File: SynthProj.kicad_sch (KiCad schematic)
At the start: 32 parts, among them J10 PWM IN, J15 Mixer Ext In, J17 S&H_In, J17 S&H_Out, J20 Ext CV, J9 Lin CV In

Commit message: more work...
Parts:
- removed J?: Master Output, SynthProjConnectors:JINJIA CK3.5-98-LF, symbol SynthProj-rescue:AudioJack2-Connector
- J?: value Master Output -> Gate Out
- J?: value Master Output -> Sequencer CV1
- J?: value Master Output -> Sequencer CV3
- J?: value Master Output -> Sequencer CV2
- J?: value Master Output -> Trigger Out
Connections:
- net SequencerAnalogGenerator/CV1: now also J?.T
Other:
- moved on the sheet: J?

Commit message: finishing schematic 1.0
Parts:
- removed J?: ADEG2_OUT, SynthProjConnectors:JINJIA CK3.5-98-LF, symbol SynthProj-rescue:AudioJack2-Connector
- added J? (x8): Sequencer CV1, SynthProjConnectors:JINJIA CK3.5-98-LF, symbol SynthProj-rescue:AudioJack2-Connector
- J18: renamed from J20; value Ext CV -> Ext In
- J?: value ADEG2_OUT -> Echo_ExtIn
- J?: value ADEG2_OUT -> Echo_DV
- J?: value ADEG2_OUT -> Echo_CV_In
- J?: value ADEG2_OUT -> Echo_Repeat
- renumbered J15 to J?, J17 to J?, J9 to J?, J10 to J?
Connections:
- net GNDREF: now also J?.S, J?.S, J?.S, J?.S, J?.S, J?.S, J?.S, J?.S
- new net RP2040Microcontroller/VIN_A: J?.T
- new net RP2040Microcontroller/VIN_B: J?.T
- new net RP2040Microcontroller/VIN_C: J?.T
- new net RP2040Microcontroller/VIN_D: J?.T
- new net RP2040Microcontroller/VOUT_A: J?.T
- new net RP2040Microcontroller/VOUT_B: J?.T
- new net RP2040Microcontroller/VOUT_C: J?.T
- new net RP2040Microcontroller/VOUT_D: J?.T
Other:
- sheet PT2399Echo ports: added none; removed VCA
- sheet RP2040Microcontroller ports: added VIN_A, VIN_B, VIN_C, VIN_D, VOUT_A, VOUT_B, VOUT_C, VOUT_D; removed none
- note added: "100k 20mm Linear Pot: RK09D1130-F20-C0-B104 100k 20mm Log Pot: RK09D1130-F20-C0-A104 10k 20mm Linear Pot: RK09D1130-F20-C0-B103 10k 20mm Log Pot: RK09D1130-F20-C0-V103"
- note added: "12 Pole Rotary Switch - Metal MC12L1NCQD 9.4mm shoulder height 12 Pole Rotary Switch - Plastic RTAP31S12W25FS 12.6mm shoulder height 12 Pole Rotary Switch - Plastic KC52A10.001NPS 14.2mm shoulder height 12 Pole Rotary Switch - Plastic SR2612F-0112-21R0B-D8-N 12.6mm shoulder height"
- note added: "4 Pole Rotary Switch - SRBV141404"
- note added: "Miniture switches need a panel height of 9.5 to 18.8mm."
- note added: "SPST On-Off MTS-101-A1-T0 SPDT On-On MTS-102-A01-T0 SPDT On-Off-On MTS-103-A1-T0 DPDT On-On MTS-202-A1-T0 DPDT On-Off-On MTS-203-A1-T0 I'm going to use the MTS series because it is a little bigger"
- note added: "SubMiniture switches need a panel height of 8.6 to 14.2mm."
- note added: "The panel height will hopefully be about 14-15mm off the pcb, for a total thickeness of about 16mm, then with knobs and buttons protruding."
- note added: "Vertical Midi Connector SD-50BV - Its 15.8mm tall"
- moved on the sheet: J?

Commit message: Doing some layout
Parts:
- J18, J? (x37): footprint SynthProjConnectors:JINJIA CK3.5-98-LF -> SynthProjConnectors:PJ-358

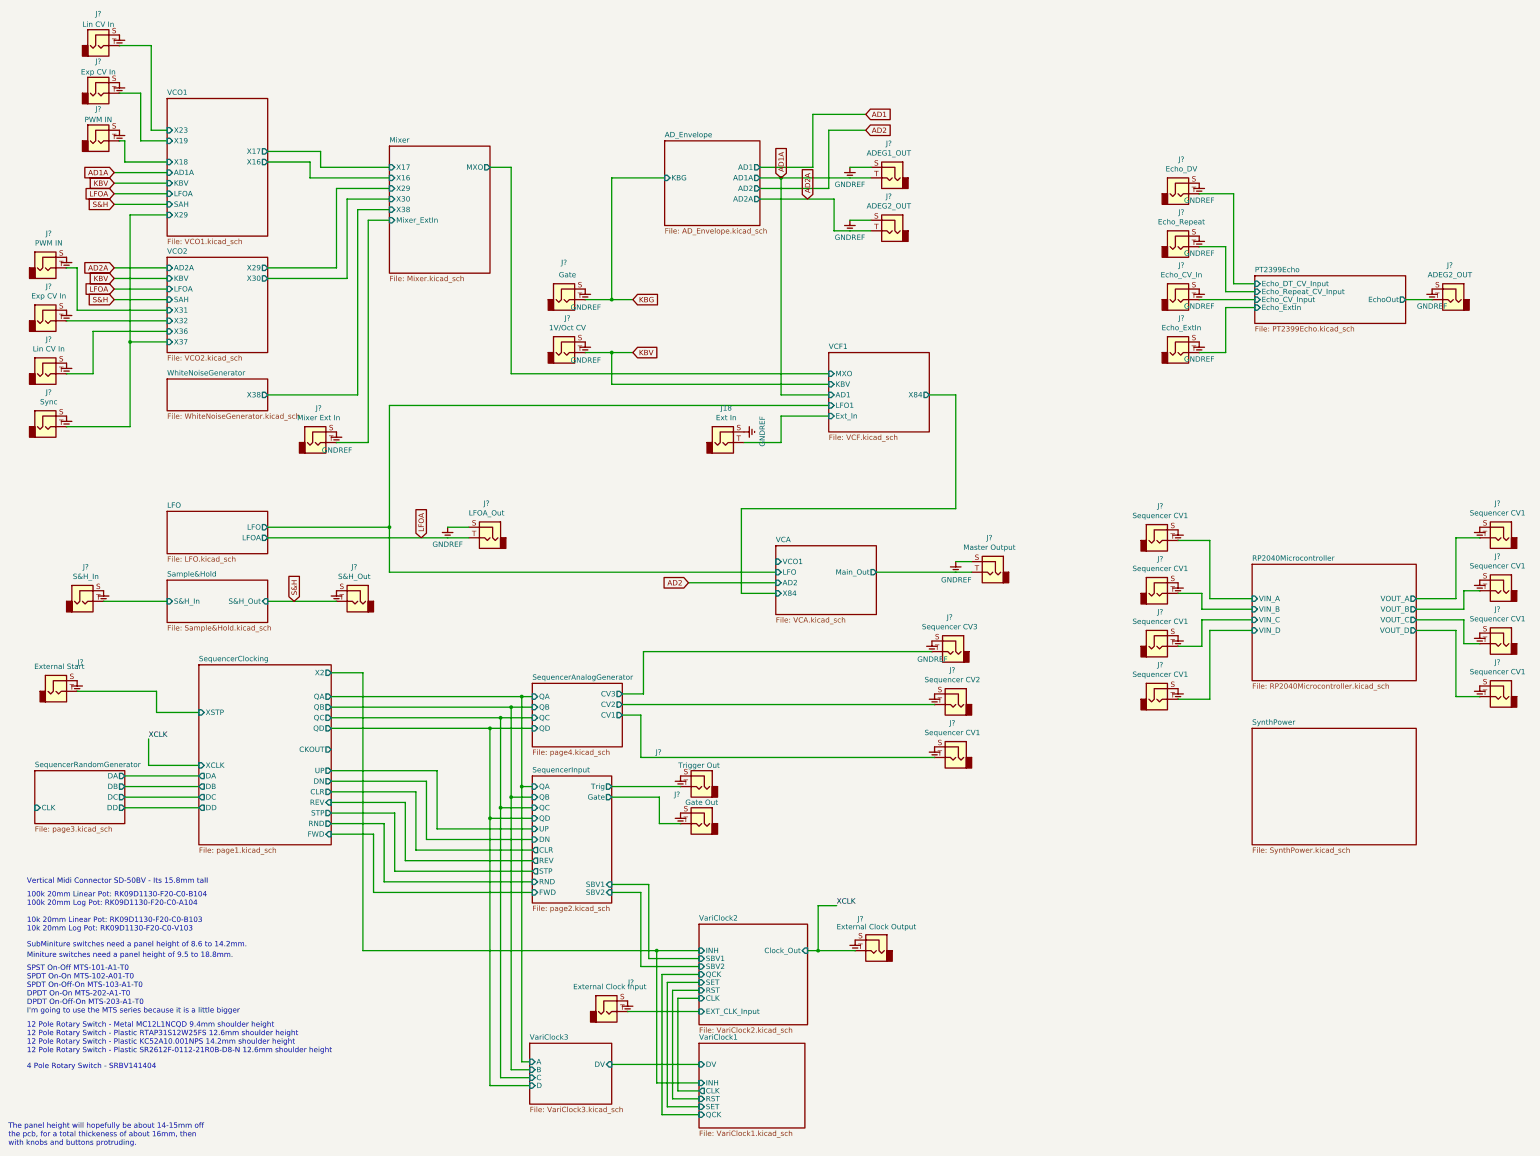
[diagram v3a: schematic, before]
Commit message: doing some routing - split sequencer into another project
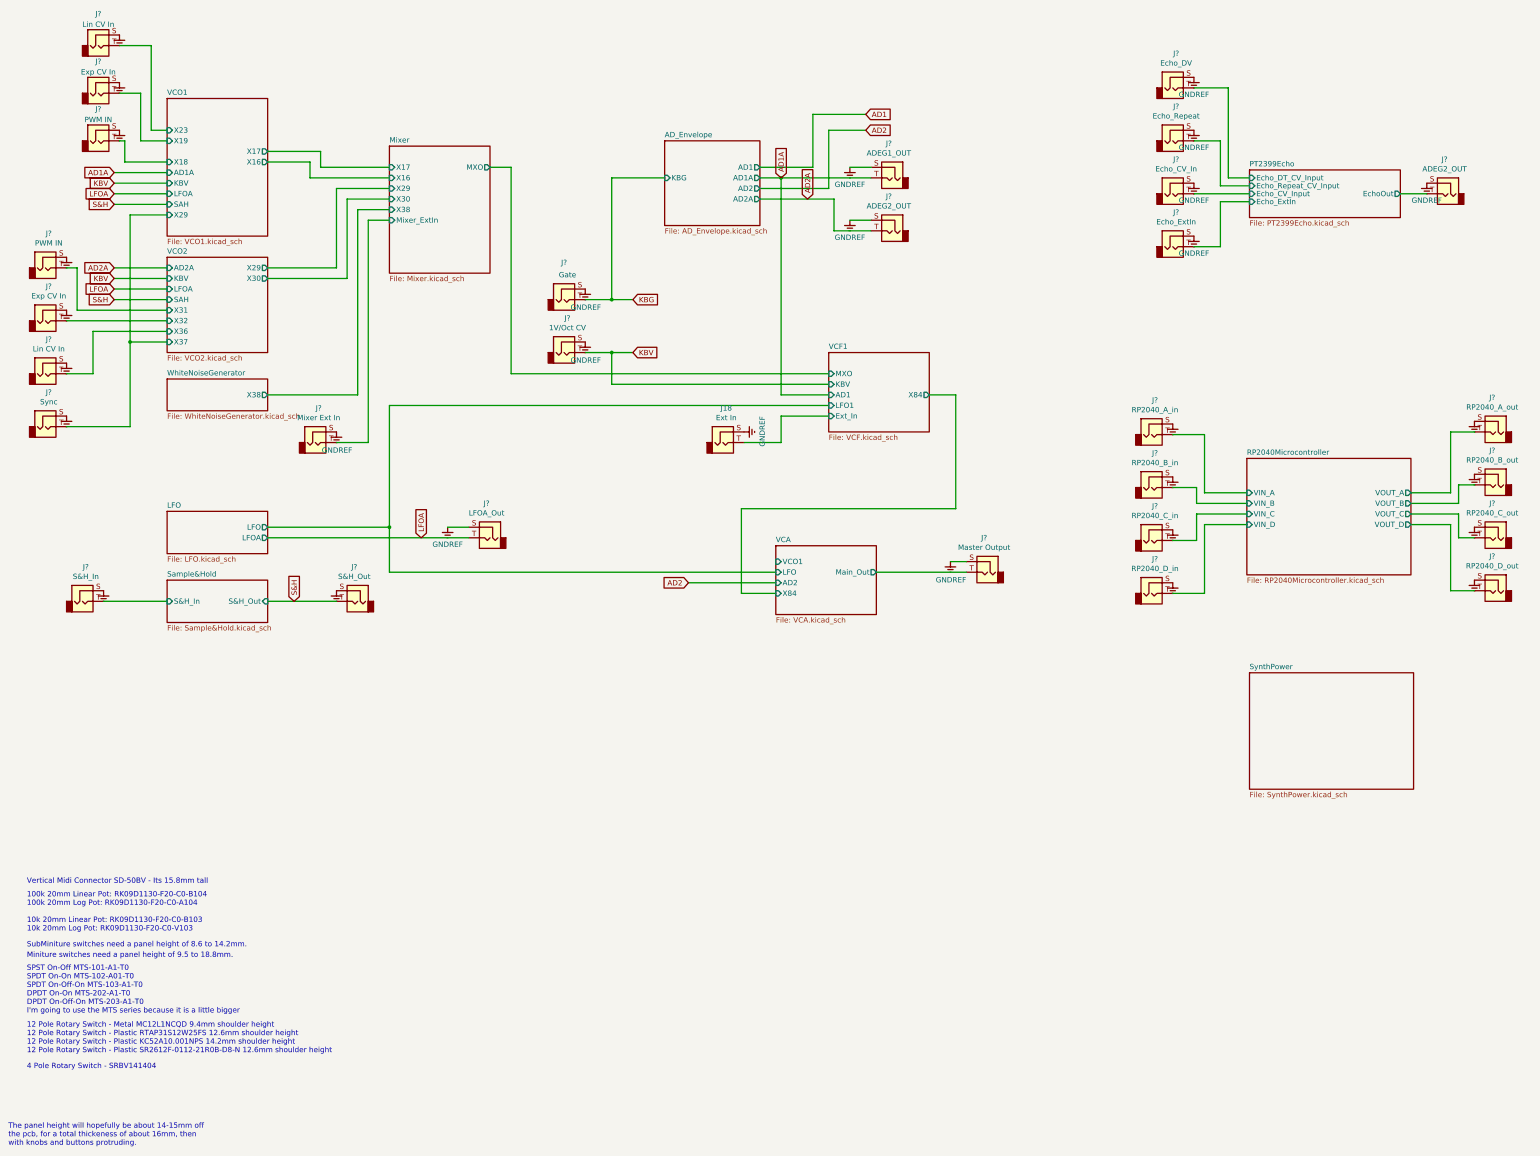
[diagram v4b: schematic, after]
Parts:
- removed J?: External Clock Output, SynthProjConnectors:PJ-358, symbol SynthProj-rescue:AudioJack2-Connector
- removed J?: Gate Out, SynthProjConnectors:PJ-358, symbol SynthProj-rescue:AudioJack2-Connector
- removed J?: Sequencer CV1, SynthProjConnectors:PJ-358, symbol SynthProj-rescue:AudioJack2-Connector
- removed J?: Sequencer CV3, SynthProjConnectors:PJ-358, symbol SynthProj-rescue:AudioJack2-Connector
- removed J?: Sequencer CV2, SynthProjConnectors:PJ-358, symbol SynthProj-rescue:AudioJack2-Connector
- removed J?: Trigger Out, SynthProjConnectors:PJ-358, symbol SynthProj-rescue:AudioJack2-Connector
- removed J?: External Start, SynthProjConnectors:PJ-358, symbol SynthProj-rescue:AudioJack2-Connector
- removed J?: External Clock Input, SynthProjConnectors:PJ-358, symbol SynthProj-rescue:AudioJack2-Connector
- J18, J? (x21): footprint SynthProjConnectors:PJ-358 -> SynthProjConnectors:PJ-301
- J?: value Sequencer CV1 -> RP2040_A_out; footprint SynthProjConnectors:PJ-358 -> SynthProjConnectors:PJ-301
- J?: value Sequencer CV1 -> RP2040_D_in; footprint SynthProjConnectors:PJ-358 -> SynthProjConnectors:PJ-301
- J?: value Sequencer CV1 -> RP2040_C_in; footprint SynthProjConnectors:PJ-358 -> SynthProjConnectors:PJ-301
- J?: value Sequencer CV1 -> RP2040_B_out; footprint SynthProjConnectors:PJ-358 -> SynthProjConnectors:PJ-301
- J?: value Sequencer CV1 -> RP2040_A_in; footprint SynthProjConnectors:PJ-358 -> SynthProjConnectors:PJ-301
- J?: value Sequencer CV1 -> RP2040_C_out; footprint SynthProjConnectors:PJ-358 -> SynthProjConnectors:PJ-301
- J?: value Sequencer CV1 -> RP2040_D_out; footprint SynthProjConnectors:PJ-358 -> SynthProjConnectors:PJ-301
- J?: value Sequencer CV1 -> RP2040_B_in; footprint SynthProjConnectors:PJ-358 -> SynthProjConnectors:PJ-301
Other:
- removed sheet SequencerAnalogGenerator
- removed sheet SequencerClocking
- removed sheet SequencerInput
- removed sheet SequencerRandomGenerator
- removed sheet VariClock1
- removed sheet VariClock2
- removed sheet VariClock3
- moved on the sheet: J?

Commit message: routing work...
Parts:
- removed J?: RP2040_D_in, SynthProjConnectors:PJ-301, symbol SynthProj-rescue:AudioJack2-Connector
- J?: value ADEG2_OUT -> ECHO_OUT
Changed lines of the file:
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@@
 (kicad_sch (version 20230121) (generator eeschema)
-  (paper "A3")
+  (paper "A4")
   (junction (at 105.41 134.62) (diameter 0) (color 0 0 0 0)
   )
@@
     (stroke (width 0) (type default))
   )
-  (wire (pts (xy 311.15 133.985) (xy 300.99 133.985))
-    (stroke (width 0) (type default))
-  )
   (wire (pts (xy 210.82 53.34) (xy 210.82 39.37))
     (stroke (width 0) (type default))
@@
     (stroke (width 0) (type default))
   )
-  (wire (pts (xy 300.99 150.495) (xy 293.37 150.495))
-    (stroke (width 0) (type default))
-  )
   (wire (pts (xy 95.25 55.88) (xy 105.41 55.88))
     (stroke (width 0) (type default))
@@
     (stroke (width 0) (type default))
   )
-  (wire (pts (xy 300.99 133.985) (xy 300.99 150.495))
-    (stroke (width 0) (type default))
-  )
   (wire (pts (xy 158.75 100.33) (xy 158.75 92.71))
     (stroke (width 0) (type default))
@@
   )
   (text "SubMiniture switches need a panel height of 8.6 to 14.2mm."
-    (at 18.415 235.585 0)
+    (at 12.7 208.915 0)
     (effects (font (size 1.27 1.27)) (justify left bottom))
   )
-  (text "Vertical Midi Connector SD-50BV - Its 15.8mm tall" (at 18.415 220.345 0)
+  (text "Vertical Midi Connector SD-50BV - Its 15.8mm tall" (at 12.7 193.675 0)
     (effects (font (size 1.27 1.27)) (justify left bottom))
   )
   (text "100k 20mm Linear Pot: RK09D1130-F20-C0-B104\n100k 20mm Log Pot: RK09D1130-F20-C0-A104\n\n10k 20mm Linear Pot: RK09D1130-F20-C0-B103\n10k 20mm Log Pot: RK09D1130-F20-C0-V103"
-    (at 18.415 231.775 0)
+    (at 12.7 205.105 0)
     (effects (font (size 1.27 1.27)) (justify left bottom))
   )
-  (text "4 Pole Rotary Switch - SRBV141404\n" (at 18.415 264.795 0)
+  (text "4 Pole Rotary Switch - SRBV141404\n" (at 12.7 238.125 0)
     (effects (font (size 1.27 1.27)) (justify left bottom))
   )
   (text "The panel height will hopefully be about 14-15mm off \nthe pcb, for a total thickeness of about 16mm, then \nwith knobs and buttons protruding.\n"
-    (at 13.97 283.21 0)
+    (at 8.255 256.54 0)
     (effects (font (size 1.27 1.27)) (justify left bottom))
   )
   (text "SPST On-Off MTS-101-A1-T0\nSPDT On-On MTS-102-A01-T0\nSPDT On-Off-On MTS-103-A1-T0\nDPDT On-On MTS-202-A1-T0\nDPDT On-Off-On MTS-203-A1-T0\nI'm going to use the MTS series because it is a little bigger"
-    (at 18.415 251.46 0)
+    (at 12.7 224.79 0)
     (effects (font (size 1.27 1.27)) (justify left bottom))
   )
   (text "Miniture switches need a panel height of 9.5 to 18.8mm."
-    (at 18.415 238.125 0)
+    (at 12.7 211.455 0)
     (effects (font (size 1.27 1.27)) (justify left bottom))
   )
   (text "12 Pole Rotary Switch - Metal MC12L1NCQD 9.4mm shoulder height\n12 Pole Rotary Switch - Plastic RTAP31S12W25FS 12.6mm shoulder height\n12 Pole Rotary Switch - Plastic KC52A10.001NPS 14.2mm shoulder height\n12 Pole Rotary Switch - Plastic SR2612F-0112-21R0B-D8-N 12.6mm shoulder height "
-    (at 18.415 260.985 0)
+    (at 12.7 234.315 0)
     (effects (font (size 1.27 1.27)) (justify left bottom))
   )
@@
     )
   )
-  (symbol (lib_id "SynthProj-rescue:AudioJack2-Connector") (at 288.29 150.495 0) (unit 1)
-    (in_bom yes) (on_board yes) (dnp no)
-    (property "Reference" "J?" (at 289.1028 142.24 0)
-      (effects (font (size 1.27 1.27)))
-    )
-    (property "Value" "RP2040_D_in" (at 289.1028 144.5514 0)
-      (effects (font (size 1.27 1.27)))
-    )
-    (property "Footprint" "SynthProjConnectors:PJ-301" (at 288.29 150.495 0)
-      (effects (font (size 1.27 1.27)) hide)
-    )
-    (property "Datasheet" "~" (at 288.29 150.495 0)
-      (effects (font (size 1.27 1.27)) hide)
-    )
-    (pin "T")
-    (pin "S")
-    (instances
-      (project "SynthProj"
-        (path "/9021c97e-351f-4ed9-b393-50257df6a463/00000000-0000-0000-0000-00006611e0f5"
-          (reference "J?") (unit 1)
-        )
-        (path "/9021c97e-351f-4ed9-b393-50257df6a463/00000000-0000-0000-0000-0000659a4e2e"
-          (reference "J?") (unit 1)
-        )
-        (path "/9021c97e-351f-4ed9-b393-50257df6a463/00000000-0000-0000-0000-000066d02a14"
-          (reference "J?") (unit 1)
-        )
-        (path "/9021c97e-351f-4ed9-b393-50257df6a463"
-          (reference "J29") (unit 1)
-        )
-      )
-    )
-  )
   (symbol (lib_id "power:GNDREF") (at 27.94 95.25 0) (unit 1)
     (in_bom yes) (on_board yes) (dnp no)
@@
       (effects (font (size 1.27 1.27)))
     )
-    (property "Value" "ADEG2_OUT" (at 358.5972 48.6664 0)
+    (property "Value" "ECHO_OUT" (at 358.5972 48.6664 0)
       (effects (font (size 1.27 1.27)))
     )
@@
         )
       )
-    )
-  )
-  (symbol (lib_id "power:GNDREF") (at 293.37 147.955 0) (mirror y) (unit 1)
-    (in_bom yes) (on_board yes) (dnp no)
-    (property "Reference" "#PWR?" (at 293.37 154.305 0)
-      (effects (font (size 1.27 1.27)) hide)
-    )
-    (property "Value" "GNDREF" (at 293.243 152.3492 0)
-      (effects (font (size 1.27 1.27)) hide)
-    )
-    (property "Footprint" "" (at 293.37 147.955 0)
-      (effects (font (size 1.27 1.27)) hide)
-    )
-    (property "Datasheet" "" (at 293.37 147.955 0)
-      (effects (font (size 1.27 1.27)) hide)
-    )
-    (pin "1")
-    (instances
-      (project "SynthProj"
-        (path "/9021c97e-351f-4ed9-b393-50257df6a463/00000000-0000-0000-0000-000066d02a14"
-          (reference "#PWR?") (unit 1)
-        )
-        (path "/9021c97e-351f-4ed9-b393-50257df6a463/00000000-0000-0000-0000-00006611e0f5"
-          (reference "#PWR?") (unit 1)
-        )
-        (path "/9021c97e-351f-4ed9-b393-50257df6a463"
-          (reference "#PWR029") (unit 1)
-        )
-      )

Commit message: more routing...
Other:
- moved on the sheet: J18, J?
